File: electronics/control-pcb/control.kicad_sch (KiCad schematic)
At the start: 25 parts, among them J1 XIAO D0-D6, J2 XIAO 5V-D7, J3 USB-C board, J4 Joystick, J5 Battery, Q1 AO3401A, SW1 KSC221JLFS, SW2 KSC221JLFS, SW3 KSC221JLFS, U1 MCP73831T-2ACI/OT, U2 TPS70933DBVR

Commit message: Complete the V0.26 model with cables and keypad
Model the bought cables and their plugs and route them: joystick to
control board round the joystick board's top edge, USB-C board to the
control board in front of its rib, and the pouch's own lead straight
to a top-entry PH socket, with the pouch fitted protection board up
(27 mm of lead instead of a 76 mm run or an extension). The keypad
keys lose their back nubs so the sheet prints flat; the switches sit
in the plate holes and the upper bosses pass through the board. Board
sockets, the TVS and the fuse move to clear the plugs.

Signed-off-by: Marc Cirauqui <marc@tetrate.io>
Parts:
- J5: footprint Connector_JST:JST_PH_S2B-PH-SM4-TB_1x02-1MP_P2.00mm_Horizontal -> Connector_JST:JST_PH_B2B-PH-SM4-TB_1x02-1MP_P2.00mm_Vertical; LCSC C295747 -> C160352; MPN S2B-PH-SM4-TB(LF)(SN) -> B2B-PH-SM4-TB(LF)(SN)
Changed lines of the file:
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@@
 (wire (pts (xy 266.70 41.91) (xy 266.70 44.45)) (stroke (width 0) (type default)))
 (symbol (lib_id "power:GND") (at 266.70 44.45 0) (unit 1) (exclude_from_sim no) (in_bom no) (on_board no) (dnp no) (property "Reference" "#PWR06" (at 266.70 48.26 0) (effects (font (size 1.27 1.27)) (hide yes))) (property "Value" "GND" (at 266.70 49.53 0) (effects (font (size 1.27 1.27)))) (property "Footprint" "" (at 266.70 44.45 0) (effects (font (size 1.27 1.27)) (hide yes))) (property "Datasheet" "" (at 266.70 44.45 0) (effects (font (size 1.27 1.27)) (hide yes))) (pin "1") (instances (project "control" (path "/568ca799-ee91-5475-81fa-ed723e540657" (reference "#PWR06") (unit 1)))))
-(symbol (lib_id "Connector_Generic:Conn_01x02") (at 38.10 78.74 0) (unit 1) (exclude_from_sim no) (in_bom yes) (on_board yes) (dnp no) (property "Reference" "J5" (at 38.10 71.12 0) (effects (font (size 1.27 1.27)))) (property "Value" "Battery" (at 38.10 91.44 0) (effects (font (size 1.27 1.27)))) (property "Footprint" "Connector_JST:JST_PH_S2B-PH-SM4-TB_1x02-1MP_P2.00mm_Horizontal" (at 38.10 78.74 0) (effects (font (size 1.27 1.27)) (hide yes))) (property "Datasheet" "" (at 38.10 78.74 0) (effects (font (size 1.27 1.27)) (hide yes))) (property "Manufacturer" "JST" (at 38.10 78.74 0) (effects (font (size 1.27 1.27)) (hide yes))) (property "MPN" "S2B-PH-SM4-TB(LF)(SN)" (at 38.10 78.74 0) (effects (font (size 1.27 1.27)) (hide yes))) (property "LCSC" "C295747" (at 38.10 78.74 0) (effects (font (size 1.27 1.27)) (hide yes))) (pin "1") (pin "2") (instances (project "control" (path "/568ca799-ee91-5475-81fa-ed723e540657" (reference "J5") (unit 1)))))
+(symbol (lib_id "Connector_Generic:Conn_01x02") (at 38.10 78.74 0) (unit 1) (exclude_from_sim no) (in_bom yes) (on_board yes) (dnp no) (property "Reference" "J5" (at 38.10 71.12 0) (effects (font (size 1.27 1.27)))) (property "Value" "Battery" (at 38.10 91.44 0) (effects (font (size 1.27 1.27)))) (property "Footprint" "Connector_JST:JST_PH_B2B-PH-SM4-TB_1x02-1MP_P2.00mm_Vertical" (at 38.10 78.74 0) (effects (font (size 1.27 1.27)) (hide yes))) (property "Datasheet" "" (at 38.10 78.74 0) (effects (font (size 1.27 1.27)) (hide yes))) (property "Manufacturer" "JST" (at 38.10 78.74 0) (effects (font (size 1.27 1.27)) (hide yes))) (property "MPN" "B2B-PH-SM4-TB(LF)(SN)" (at 38.10 78.74 0) (effects (font (size 1.27 1.27)) (hide yes))) (property "LCSC" "C160352" (at 38.10 78.74 0) (effects (font (size 1.27 1.27)) (hide yes))) (property "Description" "JST PH, top entry: the battery lead leaves the board toward the pouch" (at 38.10 78.74 0) (effects (font (size 1.27 1.27)) (hide yes))) (pin "1") (pin "2") (instances (project "control" (path "/568ca799-ee91-5475-81fa-ed723e540657" (reference "J5") (unit 1)))))
 (wire (pts (xy 33.02 78.74) (xy 30.48 78.74)) (stroke (width 0) (type default)))
 (label "BAT" (at 30.48 78.74 180) (effects (font (size 1.27 1.27)) (justify right bottom)))

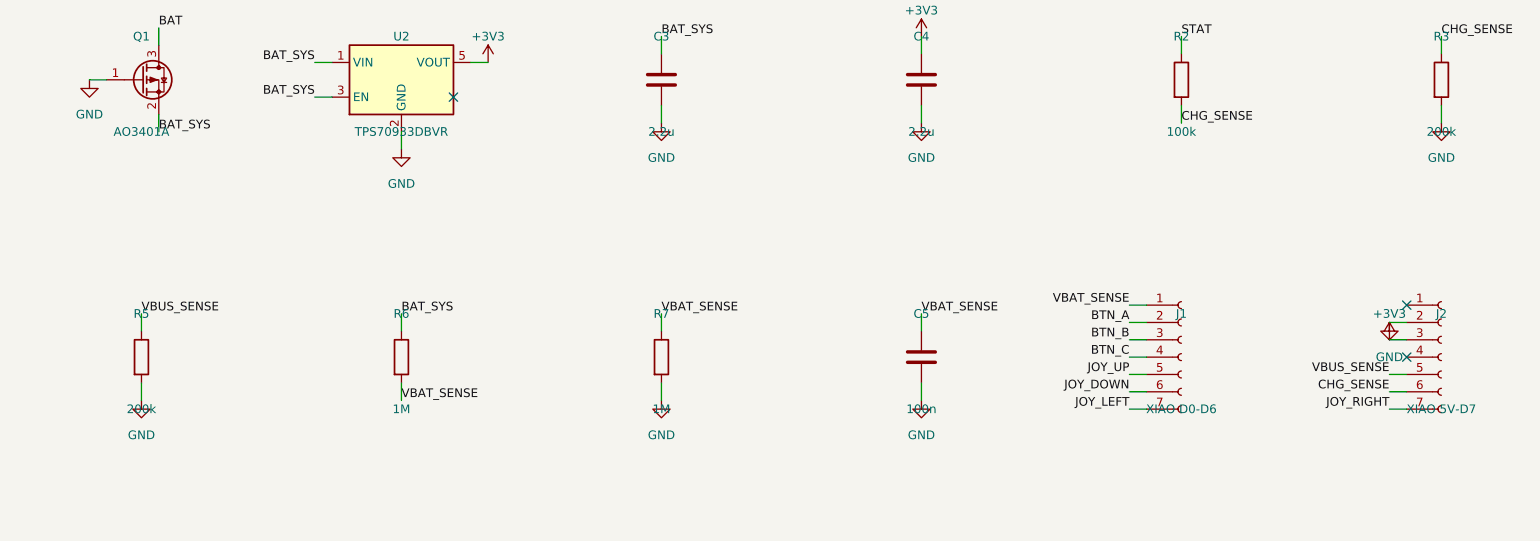
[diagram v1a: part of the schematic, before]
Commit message: Apply the control board review fixes
An independent review found no critical defect. R3 and R5 become
150k so D8 and D9 stay under the XIAO's pin limit with a low cell; C3
and C4 become 4.7 uF, above the TPS709's output minimum and the same
part as C1/C2; D1 becomes the 65 uA leakage SMBJ5.0A. The README
records the open points: charge termination with the XIAO's load,
overvoltage above the charger's rating, and a reversed cell with USB
plugged in.

Signed-off-by: Marc Cirauqui <marc@tetrate.io>
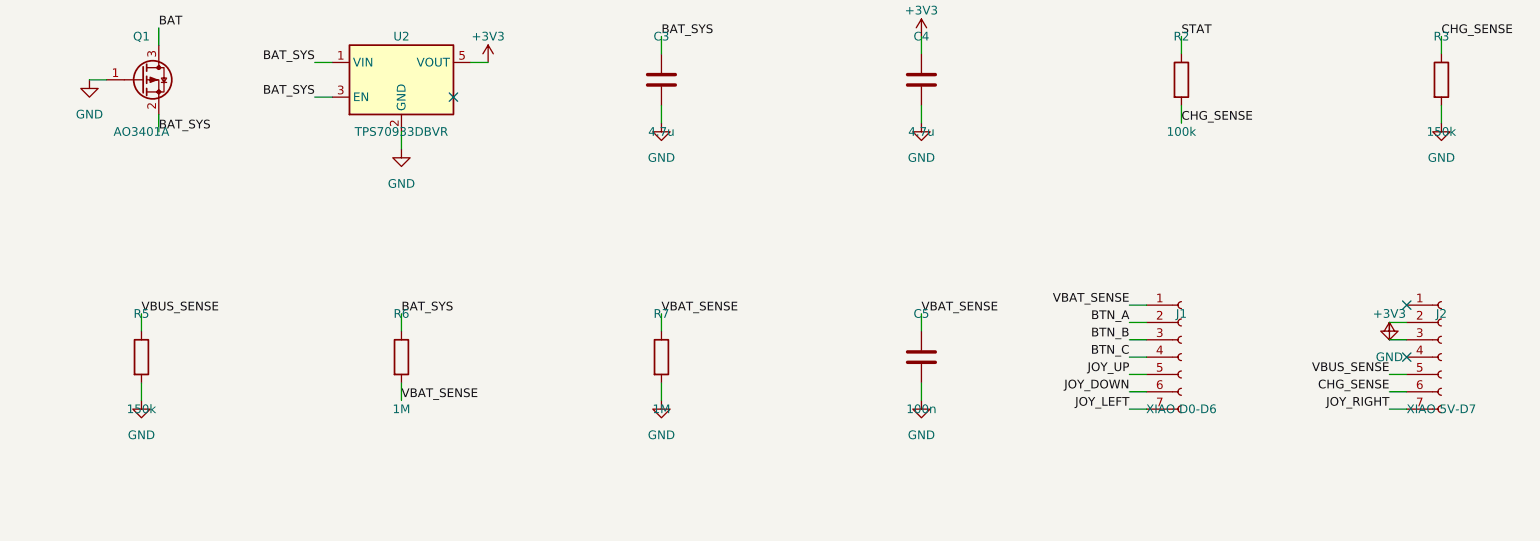
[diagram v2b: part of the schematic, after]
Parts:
- C3, C4: value 2.2u -> 4.7u; LCSC C23630 -> C19666; MPN CL10A225KO8NNNC -> CL10A475KO8NNNC
- D1: LCSC C78423 -> C83333
- R3, R5: value 200k -> 150k; LCSC C25811 -> C22807; MPN 0603WAF2003T5E -> 0603WAF1503T5E
